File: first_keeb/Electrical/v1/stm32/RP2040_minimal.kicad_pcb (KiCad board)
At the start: 4 copper layers, 67.1 x 66.8 mm, 71 parts, among them J1 Conn_01x04_Socket, P1 USB-TYPE-C-016, Q1 BSS138, SW1 TS-1187A-B-A-B, SW2 TS-1187A-B-A-B, SW3 BUTT1, SW4 BUTT3, SW5 BUTT2, U1 ME6208A44M3G, U2 ME6212C25M5G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

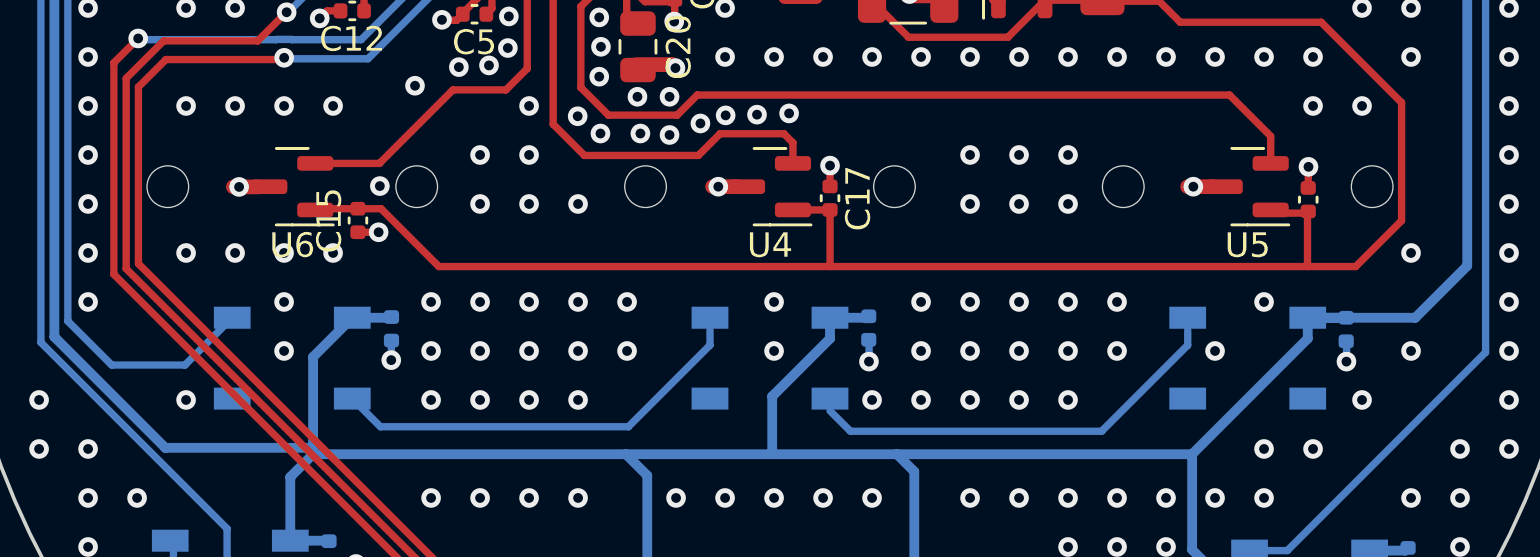
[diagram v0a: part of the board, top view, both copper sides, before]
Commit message: moves plates together
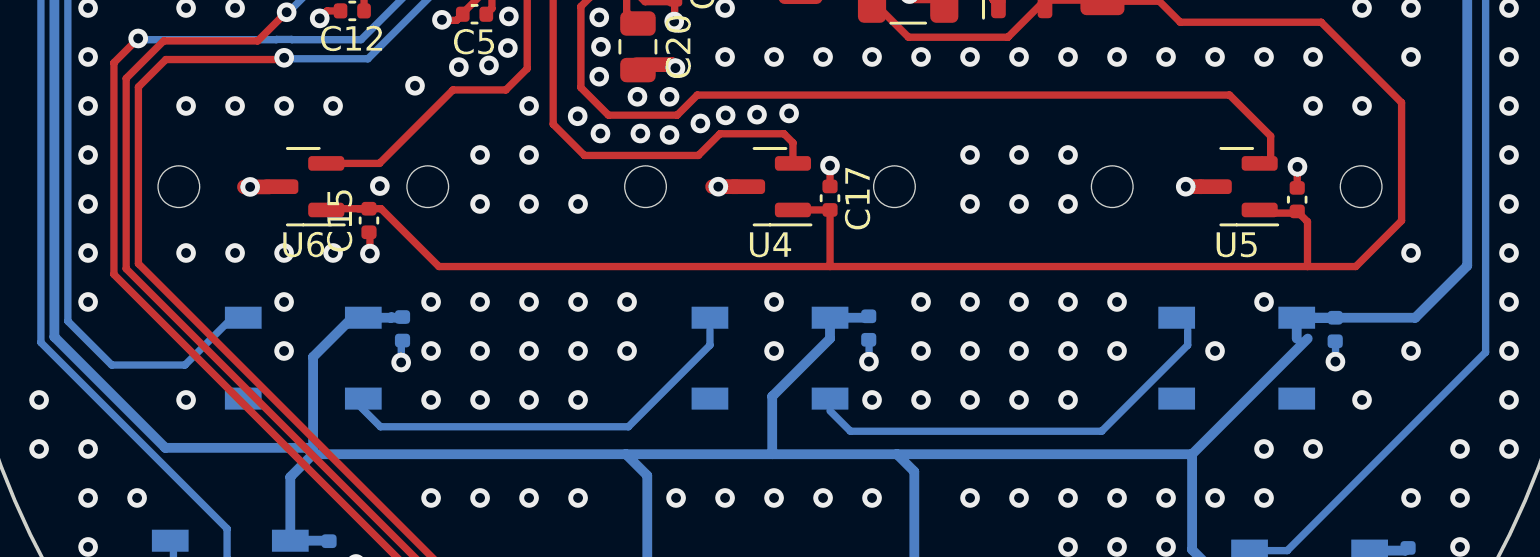
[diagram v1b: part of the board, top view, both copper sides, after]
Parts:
- moved C16 0.45 mm to (121.5, 100.5)
- moved C21 0.45 mm to (85.0, 105.8)
- moved C23 0.45 mm to (123.1, 105.8)
- moved D1 0.45 mm to (81.0, 107.0)
- moved D3 0.45 mm to (119.0, 107.0)
- moved REF** 0.45 mm to (119.0, 100.0)
- moved REF** 0.45 mm to (81.0, 100.0)
- moved U5 0.45 mm to (119.0, 100.0)
- moved U6 0.45 mm to (81.0, 100.0)
- moved C15 0.45 mm to (83.6, 101.4)

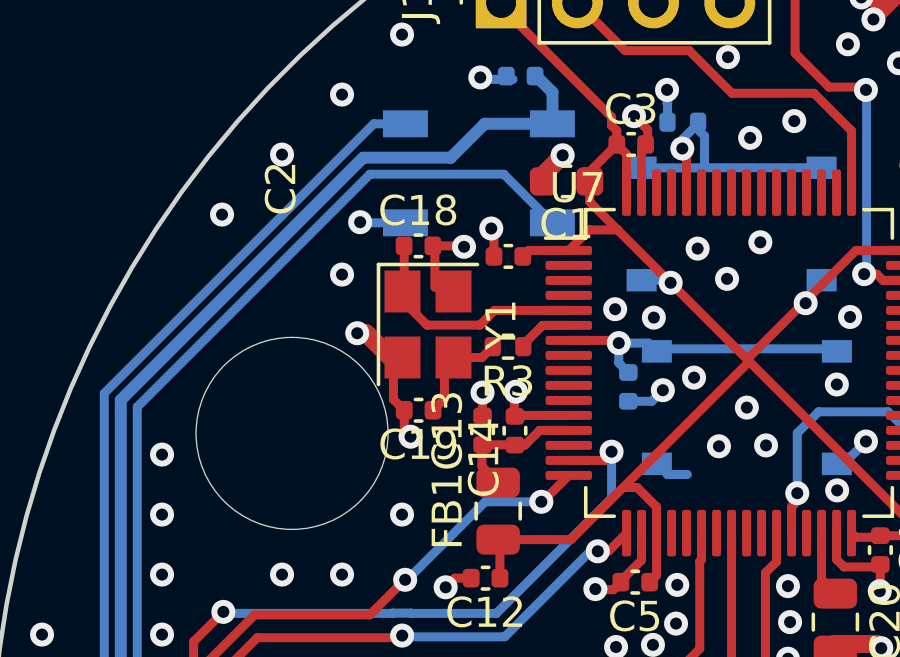
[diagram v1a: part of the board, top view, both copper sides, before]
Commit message: changes caps to match 12MHz crystal
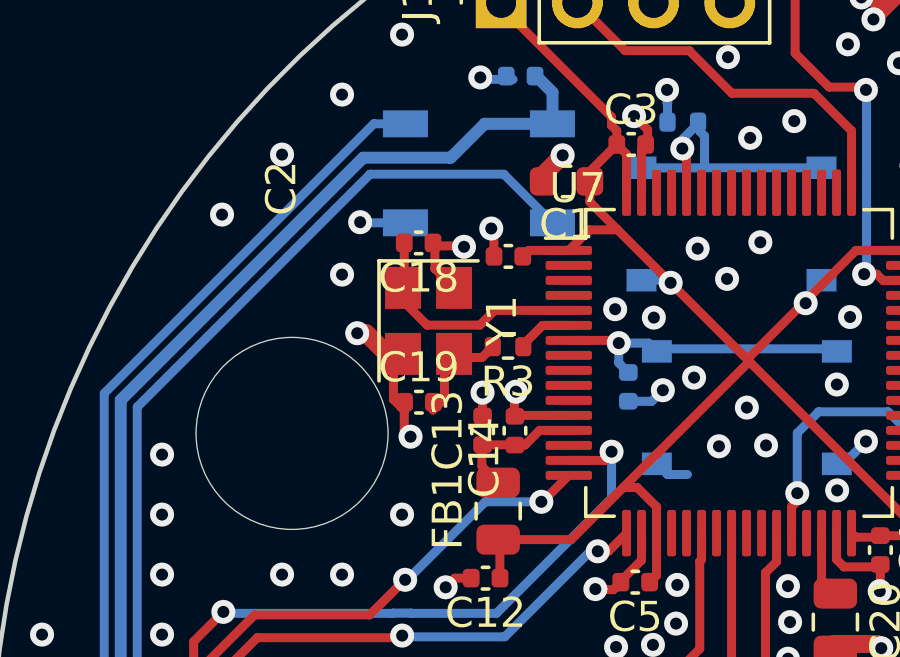
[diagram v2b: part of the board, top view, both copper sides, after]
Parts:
- C18, C19: value 12p -> 27p
- Y1: value 8MHz -> 12MHz
- moved C19 0.27 mm to (80.7, 87.0), turned to 0 degrees
- moved Y1 0.12 mm to (81.0, 84.2)
- moved C18 0.10 mm to (80.7, 81.7), turned to 180 degrees
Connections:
- C18 pad 1: OSC_IN -> GND
- C18 pad 2: GND -> OSC_IN
- C19 pad 1: Net-(C19-Pad1) -> GND
- C19 pad 2: GND -> Net-(C19-Pad2)
- R3 pad 2: Net-(C19-Pad1) -> Net-(C19-Pad2)
- Y1 pad 3: Net-(C19-Pad1) -> Net-(C19-Pad2)
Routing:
- net Net-(C19-Pad2): track 0.00 -> 4.28 mm
- net Net-(C19-Pad1): track 4.28 -> 0.00 mm
